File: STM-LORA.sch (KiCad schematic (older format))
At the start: 16 parts, among them J1 Batt, J2 Solar, J3 CONN_01X17, J4 CONN_01X03, J5 CONN_01X03, J6 CONN_01X01, J7 CONN_01X14, J8 CONN_01X05, J9 CONN_01X05, U1 stm32f103c8t6-module-china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

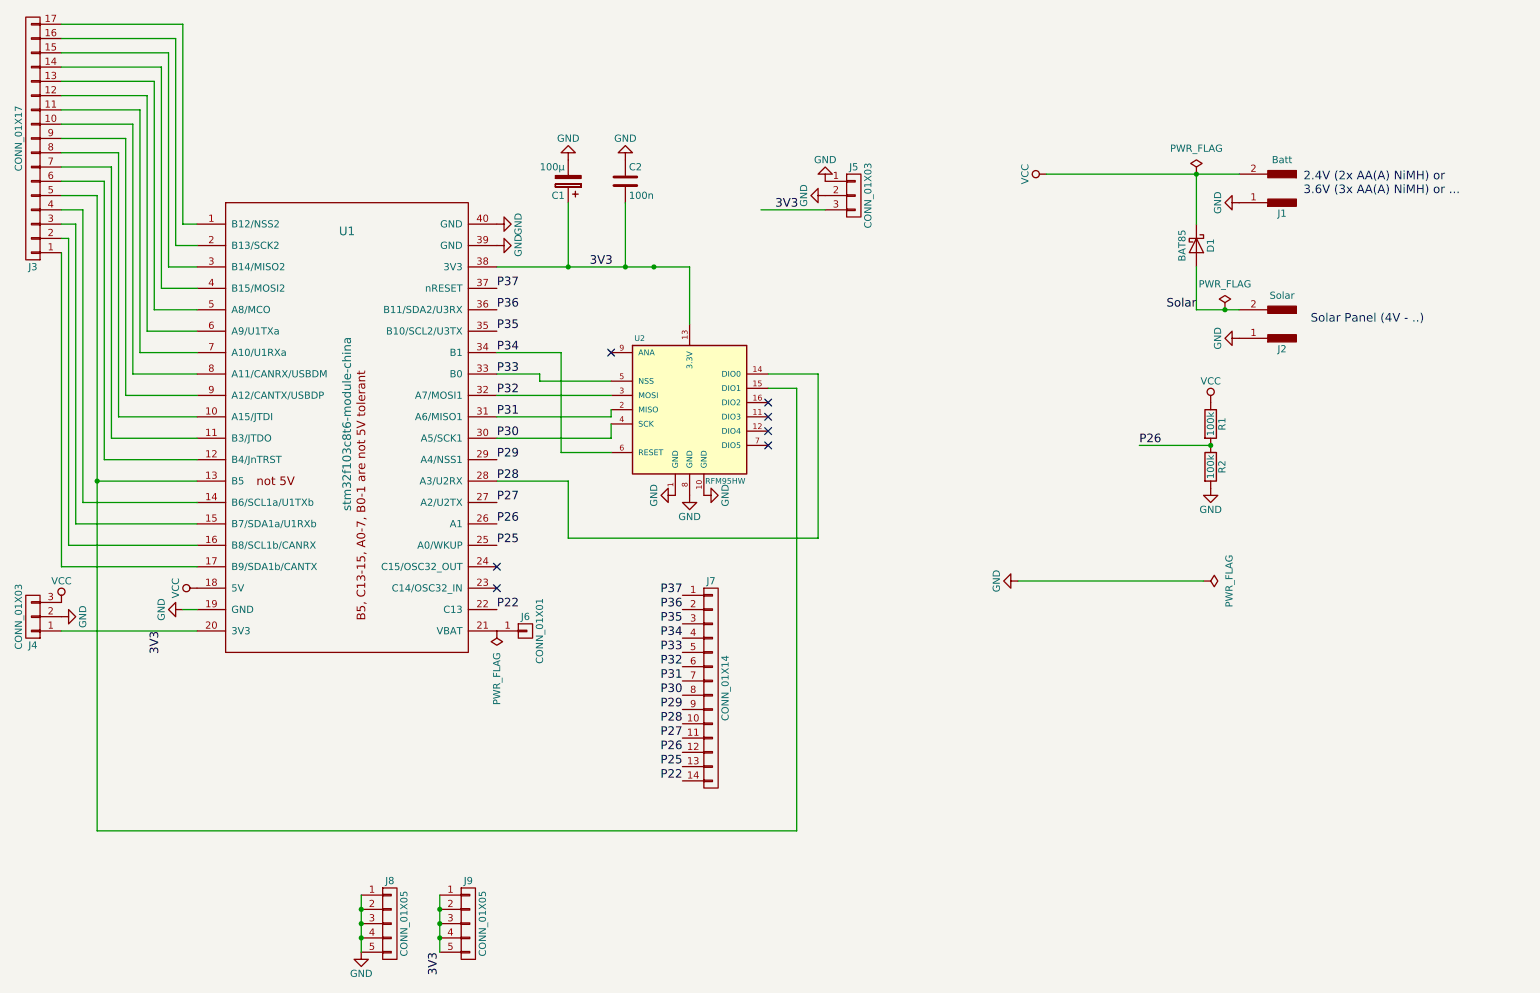
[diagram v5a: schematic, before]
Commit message: Change and add exp headers to schema (0.2)
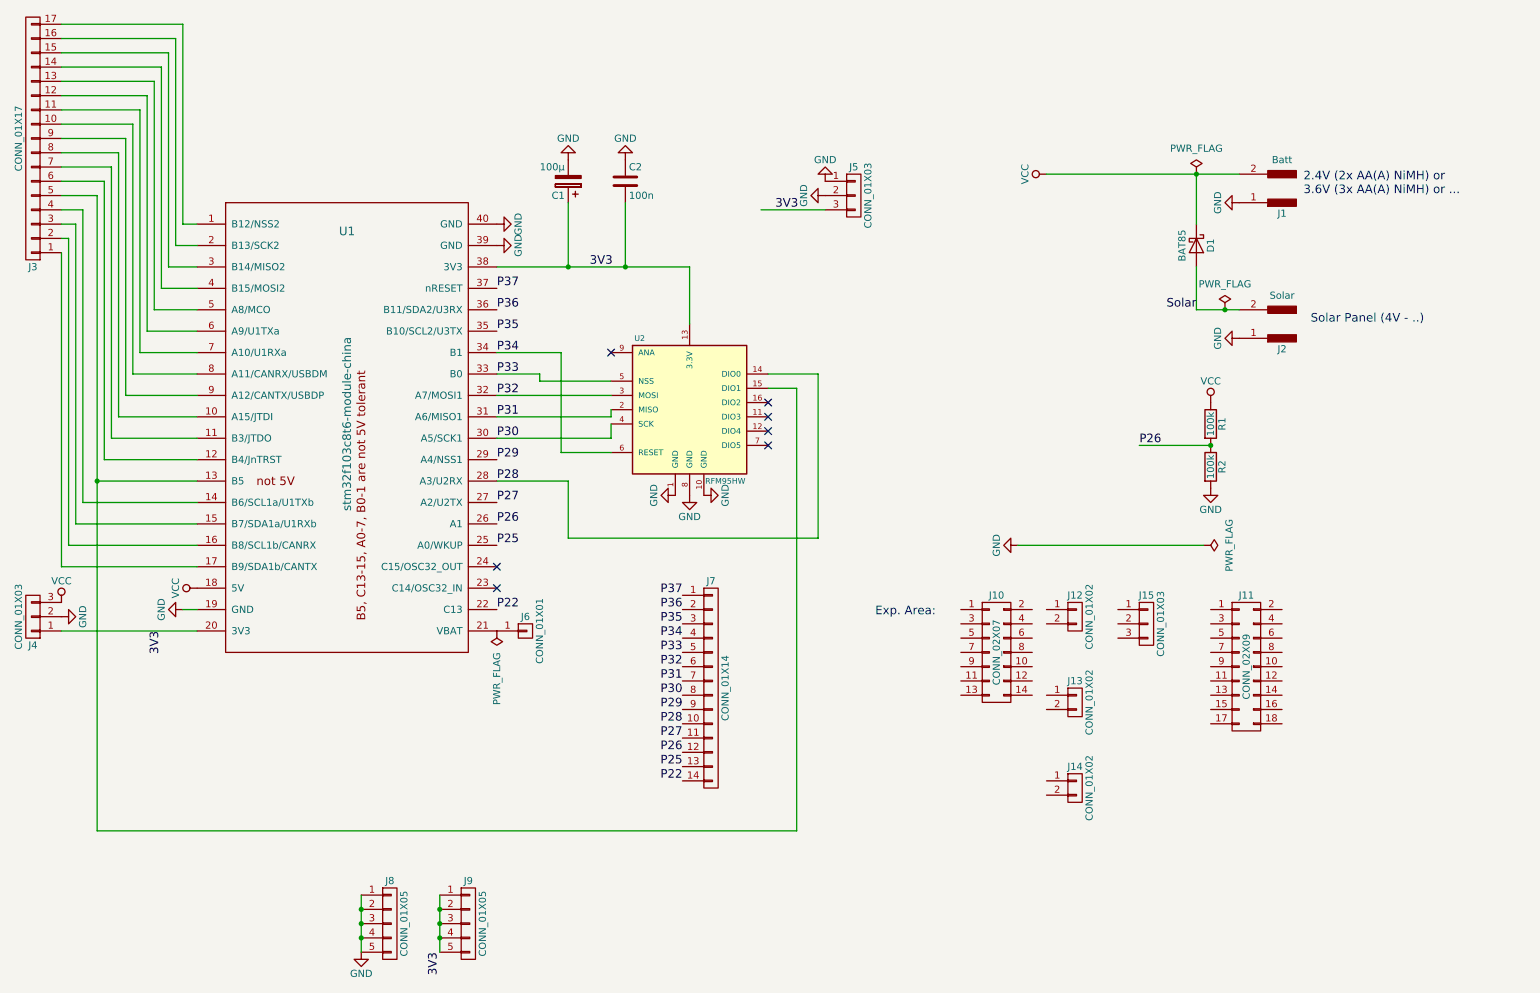
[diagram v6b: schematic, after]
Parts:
- added J10: CONN_02X07, Pin_Headers:Pin_Header_Straight_2x07_Pitch2.54mm, symbol CONN_02X07
- added J11: CONN_02X09, Pin_Headers:Pin_Header_Straight_2x09_Pitch2.54mm, symbol CONN_02X09
- added J12, J13, J14: CONN_01X02, Pin_Headers:Pin_Header_Straight_1x02_Pitch2.54mm, symbol CONN_01X02
- added J15: CONN_01X03, Pin_Headers:Pin_Header_Straight_1x03_Pitch2.54mm, symbol CONN_01X03
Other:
- note added: "Exp. Area:"
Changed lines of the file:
@@
 Title "STM32 RFM95 Proto Board"
 Date "2017-04-01"
-Rev "0.1"
+Rev "0.2"
 Comp "http://v7f.eu"
 Comment1 ""
@@
 L GND #PWR08
 U 1 1 58DF686D
-P 7550 4750
-F 0 "#PWR08" H 7550 4500 50  0001 C CNN
-F 1 "GND" H 7550 4600 50  0000 C CNN
-F 2 "" H 7550 4750 50  0000 C CNN
-F 3 "" H 7550 4750 50  0000 C CNN
-	1    7550 4750
+P 7550 4500
+F 0 "#PWR08" H 7550 4250 50  0001 C CNN
+F 1 "GND" H 7550 4350 50  0000 C CNN
+F 2 "" H 7550 4500 50  0000 C CNN
+F 3 "" H 7550 4500 50  0000 C CNN
+	1    7550 4500
 	0    1    1    0
 $EndComp
@@
 L PWR_FLAG #FLG011
 U 1 1 58DF7179
-P 8850 4750
-F 0 "#FLG011" H 8850 4845 50  0001 C CNN
-F 1 "PWR_FLAG" H 8850 4930 50  0000 C CNN
-F 2 "" H 8850 4750 50  0000 C CNN
-F 3 "" H 8850 4750 50  0000 C CNN
-	1    8850 4750
+P 8850 4500
+F 0 "#FLG011" H 8850 4595 50  0001 C CNN
+F 1 "PWR_FLAG" H 8850 4680 50  0000 C CNN
+F 2 "" H 8850 4500 50  0000 C CNN
+F 3 "" H 8850 4500 50  0000 C CNN
+	1    8850 4500
 	0    1    1    0
 $EndComp
@@
 $EndComp
 Wire Wire Line
-	7750 1900 9100 1900
+	7750 1900 8800 1900
+Wire Wire Line
+	8800 1900 9100 1900
 Wire Wire Line
 	3900 3600 4700 3600
@@
 	6000 6500 1100 6500
 Wire Wire Line
-	1100 6500 1100 2050
+	1100 6500 1100 4050
+Wire Wire Line
+	1100 4050 1100 2050
 Wire Wire Line
 	1100 4050 1800 4050
@@
 	8800 1900 8800 2250
 Wire Wire Line
-	8800 2850 9100 2850
-Wire Wire Line
-	7550 4750 8850 4750
+	8800 2850 9000 2850
+Wire Wire Line
+	9000 2850 9100 2850
+Wire Wire Line
+	7550 4500 8850 4500
 Connection ~ 9000 2850
 Wire Wire Line
@@
 	1700 4950 1800 4950
 Wire Wire Line
-	3900 2550 5250 2550
+	3900 2550 4400 2550
+Wire Wire Line
+	4400 2550 4800 2550
+Wire Wire Line
+	4800 2550 5250 2550
 Wire Wire Line
 	5250 2550 5250 2950
@@
 Wire Wire Line
 	4700 3750 3900 3750
-Connection ~ 5000 2550
 Connection ~ 4400 2550
 Connection ~ 4800 2550
@@
 	5750 2150 6200 2150
 Wire Wire Line
-	2950 6950 2950 7350
+	2950 6950 2950 7050
+Wire Wire Line
+	2950 7050 2950 7150
+Wire Wire Line
+	2950 7150 2950 7250
+Wire Wire Line
+	2950 7250 2950 7350
 Connection ~ 2950 7050
 Connection ~ 2950 7150
@@
 $EndComp
 Wire Wire Line
-	3500 6950 3500 7350
+	3500 6950 3500 7050
+Wire Wire Line
+	3500 7050 3500 7150
+Wire Wire Line
+	3500 7150 3500 7250
+Wire Wire Line
+	3500 7250 3500 7350
 Connection ~ 3500 7050
 Connection ~ 3500 7150
@@
 Text Label 3500 7350 3    60   ~ 0
 3V3
+Text Notes 6550 5000 0    60   ~ 0
+Exp. Area:
+$Comp
+L CONN_02X07 J10
+U 1 1 58E22FE3
+P 7400 5250
+F 0 "J10" H 7400 5650 50  0000 C CNN
+F 1 "CONN_02X07" V 7400 5250 50  0000 C CNN
+F 2 "Pin_Headers:Pin_Header_Straight_2x07_Pitch2.54mm" H 7400 4050 50  0001 C CNN
+F 3 "" H 7400 4050 50  0001 C CNN
+	1    7400 5250
+	1    0    0    -1
+$EndComp
+$Comp
+L CONN_02X09 J11
+U 1 1 58E2304D
+P 9150 5350
+F 0 "J11" H 9150 5850 50  0000 C CNN
+F 1 "CONN_02X09" V 9150 5350 50  0000 C CNN
+F 2 "Pin_Headers:Pin_Header_Straight_2x09_Pitch2.54mm" H 9150 4150 50  0001 C CNN
+F 3 "" H 9150 4150 50  0001 C CNN
+	1    9150 5350
+	1    0    0    -1
+$EndComp
+$Comp
+L CONN_01X02 J12
+U 1 1 58E237FE
+P 7950 5000
+F 0 "J12" H 7950 5150 50  0000 C CNN
+F 1 "CONN_01X02" V 8050 5000 50  0000 C CNN
+F 2 "Pin_Headers:Pin_Header_Straight_1x02_Pitch2.54mm" H 7950 5000 50  0001 C CNN
+F 3 "" H 7950 5000 50  0001 C CNN
+	1    7950 5000
+	1    0    0    -1
+$EndComp
+$Comp
+L CONN_01X02 J13
+U 1 1 58E23852
+P 7950 5600
+F 0 "J13" H 7950 5750 50  0000 C CNN
+F 1 "CONN_01X02" V 8050 5600 50  0000 C CNN
+F 2 "Pin_Headers:Pin_Header_Straight_1x02_Pitch2.54mm" H 7950 5600 50  0001 C CNN
+F 3 "" H 7950 5600 50  0001 C CNN
+	1    7950 5600
+	1    0    0    -1
+$EndComp
+$Comp
+L CONN_01X02 J14
+U 1 1 58E238BA
+P 7950 6200
+F 0 "J14" H 7950 6350 50  0000 C CNN
+F 1 "CONN_01X02" V 8050 6200 50  0000 C CNN
+F 2 "Pin_Headers:Pin_Header_Straight_1x02_Pitch2.54mm" H 7950 6200 50  0001 C CNN
+F 3 "" H 7950 6200 50  0001 C CNN
+	1    7950 6200
+	1    0    0    -1
+$EndComp
+$Comp
+L CONN_01X03 J15
+U 1 1 58E239DC
+P 8450 5050
+F 0 "J15" H 8450 5250 50  0000 C CNN
+F 1 "CONN_01X03" V 8550 5050 50  0000 C CNN
+F 2 "Pin_Headers:Pin_Header_Straight_1x03_Pitch2.54mm" H 8450 5050 50  0001 C CNN
+F 3 "" H 8450 5050 50  0001 C CNN
+	1    8450 5050
+	1    0    0    -1
+$EndComp
 $EndSCHEMATC

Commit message: Add NC to exp area
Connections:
- no-connect marks 7 -> 48
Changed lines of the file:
@@
 $EndComp
 Wire Wire Line
-	7750 1900 8800 1900
-Wire Wire Line
-	8800 1900 9100 1900
+	7750 1900 9100 1900
 Wire Wire Line
 	3900 3600 4700 3600
@@
 	6000 6500 1100 6500
 Wire Wire Line
-	1100 6500 1100 4050
-Wire Wire Line
-	1100 4050 1100 2050
+	1100 6500 1100 2050
 Wire Wire Line
 	1100 4050 1800 4050
@@
 	8800 1900 8800 2250
 Wire Wire Line
-	8800 2850 9000 2850
-Wire Wire Line
-	9000 2850 9100 2850
+	8800 2850 9100 2850
 Wire Wire Line
 	7550 4500 8850 4500
@@
 	1700 4950 1800 4950
 Wire Wire Line
-	3900 2550 4400 2550
-Wire Wire Line
-	4400 2550 4800 2550
-Wire Wire Line
-	4800 2550 5250 2550
+	3900 2550 5250 2550
 Wire Wire Line
 	5250 2550 5250 2950
@@
 	5750 2150 6200 2150
 Wire Wire Line
-	2950 6950 2950 7050
-Wire Wire Line
-	2950 7050 2950 7150
-Wire Wire Line
-	2950 7150 2950 7250
-Wire Wire Line
-	2950 7250 2950 7350
+	2950 6950 2950 7350
 Connection ~ 2950 7050
 Connection ~ 2950 7150
@@
 $EndComp
 Wire Wire Line
-	3500 6950 3500 7050
-Wire Wire Line
-	3500 7050 3500 7150
-Wire Wire Line
-	3500 7150 3500 7250
-Wire Wire Line
-	3500 7250 3500 7350
+	3500 6950 3500 7350
 Connection ~ 3500 7050
 Connection ~ 3500 7150
@@
 	1    0    0    -1
 $EndComp
+NoConn ~ 7150 4950
+NoConn ~ 7150 5050
+NoConn ~ 7150 5150
+NoConn ~ 7150 5250
+NoConn ~ 7150 5350
+NoConn ~ 7150 5450
+NoConn ~ 7150 5550
+NoConn ~ 7650 4950
+NoConn ~ 7650 5050
+NoConn ~ 7650 5150
+NoConn ~ 7650 5250
+NoConn ~ 7650 5350
+NoConn ~ 7650 5450
+NoConn ~ 7650 5550
+NoConn ~ 7750 4950
+NoConn ~ 7750 5050
+NoConn ~ 7750 5550
+NoConn ~ 7750 5650
+NoConn ~ 7750 6150
+NoConn ~ 7750 6250
+NoConn ~ 8250 4950
+NoConn ~ 8250 5050
+NoConn ~ 8250 5150
+NoConn ~ 8900 4950
+NoConn ~ 8900 5050
+NoConn ~ 8900 5150
+NoConn ~ 8900 5250
+NoConn ~ 8900 5350
+NoConn ~ 8900 5450
+NoConn ~ 8900 5550
+NoConn ~ 8900 5650
+NoConn ~ 8900 5750
+NoConn ~ 9400 4950
+NoConn ~ 9400 5050
+NoConn ~ 9400 5150
+NoConn ~ 9400 5250
+NoConn ~ 9400 5350
+NoConn ~ 9400 5450
+NoConn ~ 9400 5550
+NoConn ~ 9400 5650
+NoConn ~ 9400 5750
 $EndSCHEMATC

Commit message: layout silk screen
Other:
- moved on the sheet: J15
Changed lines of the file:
@@
 LIBS:stm32f103c8t6-module-china
 LIBS:RFM95
-LIBS:STM-LORA-cache
 EELAYER 25 0
 EELAYER END
@@
 $EndComp
 Wire Wire Line
-	7750 1900 9100 1900
+	7750 1900 8800 1900
+Wire Wire Line
+	8800 1900 9100 1900
 Wire Wire Line
 	3900 3600 4700 3600
@@
 	6000 6500 1100 6500
 Wire Wire Line
-	1100 6500 1100 2050
+	1100 6500 1100 4050
+Wire Wire Line
+	1100 4050 1100 2050
 Wire Wire Line
 	1100 4050 1800 4050
@@
 	8800 1900 8800 2250
 Wire Wire Line
-	8800 2850 9100 2850
+	8800 2850 9000 2850
+Wire Wire Line
+	9000 2850 9100 2850
 Wire Wire Line
 	7550 4500 8850 4500
@@
 	1700 4950 1800 4950
 Wire Wire Line
-	3900 2550 5250 2550
+	3900 2550 4400 2550
+Wire Wire Line
+	4400 2550 4800 2550
+Wire Wire Line
+	4800 2550 5250 2550
 Wire Wire Line
 	5250 2550 5250 2950
@@
 	5750 2150 6200 2150
 Wire Wire Line
-	2950 6950 2950 7350
+	2950 6950 2950 7050
+Wire Wire Line
+	2950 7050 2950 7150
+Wire Wire Line
+	2950 7150 2950 7250
+Wire Wire Line
+	2950 7250 2950 7350
 Connection ~ 2950 7050
 Connection ~ 2950 7150
@@
 $EndComp
 Wire Wire Line
-	3500 6950 3500 7350
+	3500 6950 3500 7050
+Wire Wire Line
+	3500 7050 3500 7150
+Wire Wire Line
+	3500 7150 3500 7250
+Wire Wire Line
+	3500 7250 3500 7350
 Connection ~ 3500 7050
 Connection ~ 3500 7150
@@
 L CONN_01X03 J15
 U 1 1 58E239DC
-P 8450 5050
-F 0 "J15" H 8450 5250 50  0000 C CNN
-F 1 "CONN_01X03" V 8550 5050 50  0000 C CNN
-F 2 "Pin_Headers:Pin_Header_Straight_1x03_Pitch2.54mm" H 8450 5050 50  0001 C CNN
-F 3 "" H 8450 5050 50  0001 C CNN
-	1    8450 5050
+P 8500 5050
+F 0 "J15" H 8500 5250 50  0000 C CNN
+F 1 "CONN_01X03" V 8600 5050 50  0000 C CNN
+F 2 "Pin_Headers:Pin_Header_Straight_1x03_Pitch2.54mm" H 8500 5050 50  0001 C CNN
+F 3 "" H 8500 5050 50  0001 C CNN
+	1    8500 5050
 	1    0    0    -1
 $EndComp
@@
 NoConn ~ 7750 6150
 NoConn ~ 7750 6250
-NoConn ~ 8250 4950
-NoConn ~ 8250 5050
-NoConn ~ 8250 5150
+NoConn ~ 8300 4950
+NoConn ~ 8300 5050
+NoConn ~ 8300 5150
 NoConn ~ 8900 4950
 NoConn ~ 8900 5050
